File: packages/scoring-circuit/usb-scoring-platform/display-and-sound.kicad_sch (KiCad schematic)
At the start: 14 parts, among them J7 TST-108-02-G-D - HUB75, J8 645004114822 - panel 5V, Q1 BSS138-7-F, Q2 BSS138-7-F, U14 SN74AHCT245PWR, U15 SN74AHCT245PWR

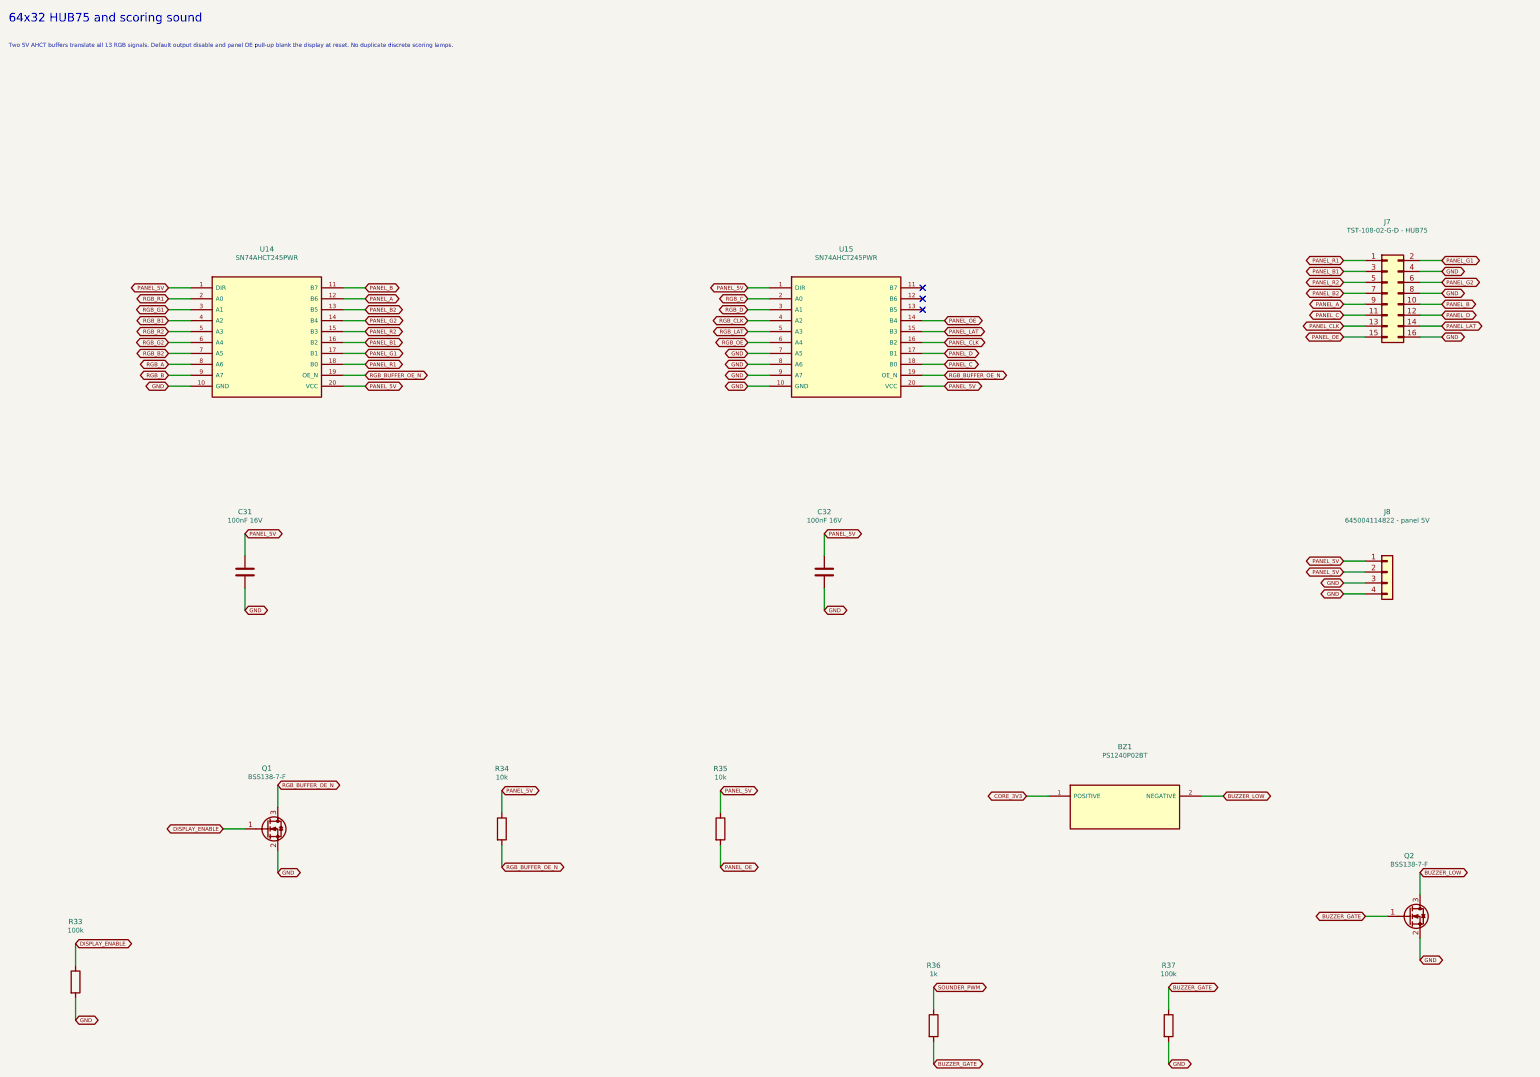
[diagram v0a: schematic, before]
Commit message: fix(scoring-circuit): define HUB75 buffer reset states
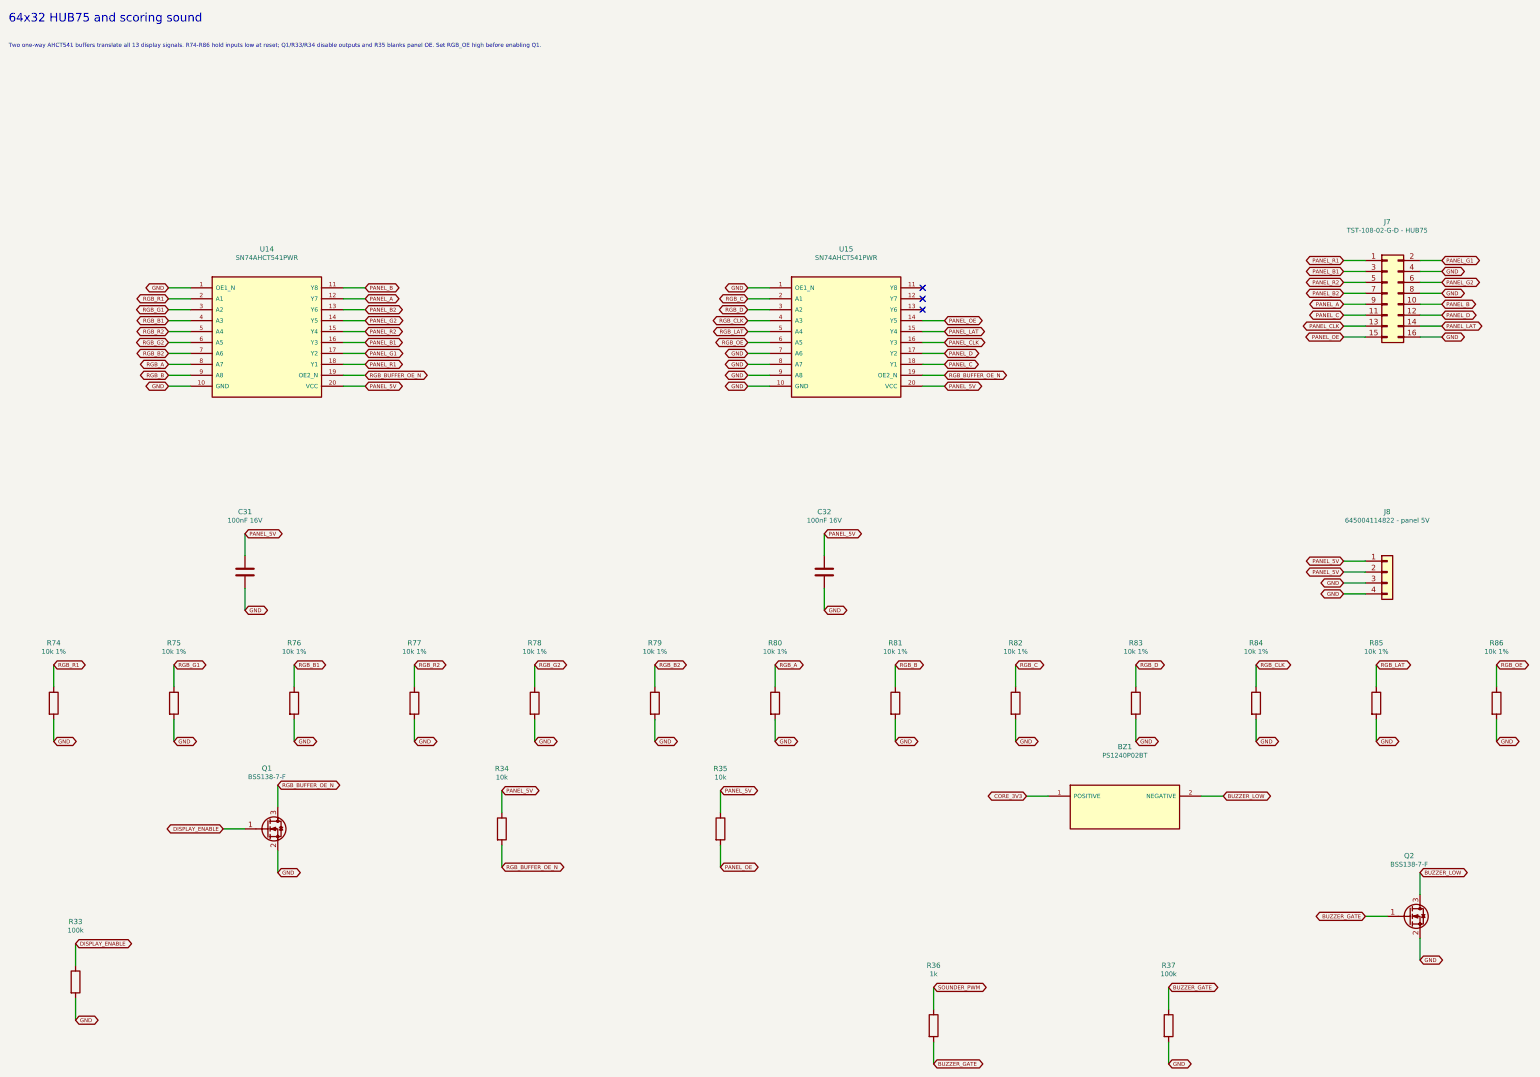
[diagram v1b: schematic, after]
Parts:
- added R74, R75, R76, R77, R78, R79, R80, R81, R82, R83, R84, R85, R86: 10k 1%, Resistor_SMD:R_0603_1608Metric, symbol Device:R
- U14, U15: value SN74AHCT245PWR -> SN74AHCT541PWR; symbol ScoringPlatform:SN74AHCT245PWR -> ScoringPlatform:SN74AHCT541PWR
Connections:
- net GND: now also U14.1 (OE1_N), U15.1 (OE1_N), R74.2, R75.2, R76.2, R77.2, R78.2, R79.2, R80.2, R81.2, R82.2, R83.2, R84.2, R85.2, R86.2
- net PANEL_5V: no longer U14.1 (DIR), U15.1 (DIR)
- net RGB_A: now also R80.1
- net RGB_B: now also R81.1
- net RGB_B1: now also R76.1
- net RGB_B2: now also R79.1
- net RGB_C: now also R82.1
- net RGB_CLK: now also R84.1
- net RGB_D: now also R83.1
- net RGB_G1: now also R75.1
- net RGB_G2: now also R78.1
- net RGB_LAT: now also R85.1
- net RGB_OE: now also R86.1
- net RGB_R1: now also R74.1
- net RGB_R2: now also R77.1
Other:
- note added: "Two one-way AHCT541 buffers translate all 13 display signals. R74-R86 hold inputs low at reset; Q1/R33/R34 disable outputs and R35 blanks panel OE. Set RGB_OE high before enabling Q1."
- note removed: "Two 5V AHCT buffers translate all 13 RGB signals. Default output disable and panel OE pull-up blank the display at reset. No duplicate discrete scoring lamps."

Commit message: fix(scoring-circuit): complete piezo sounder drive and routing
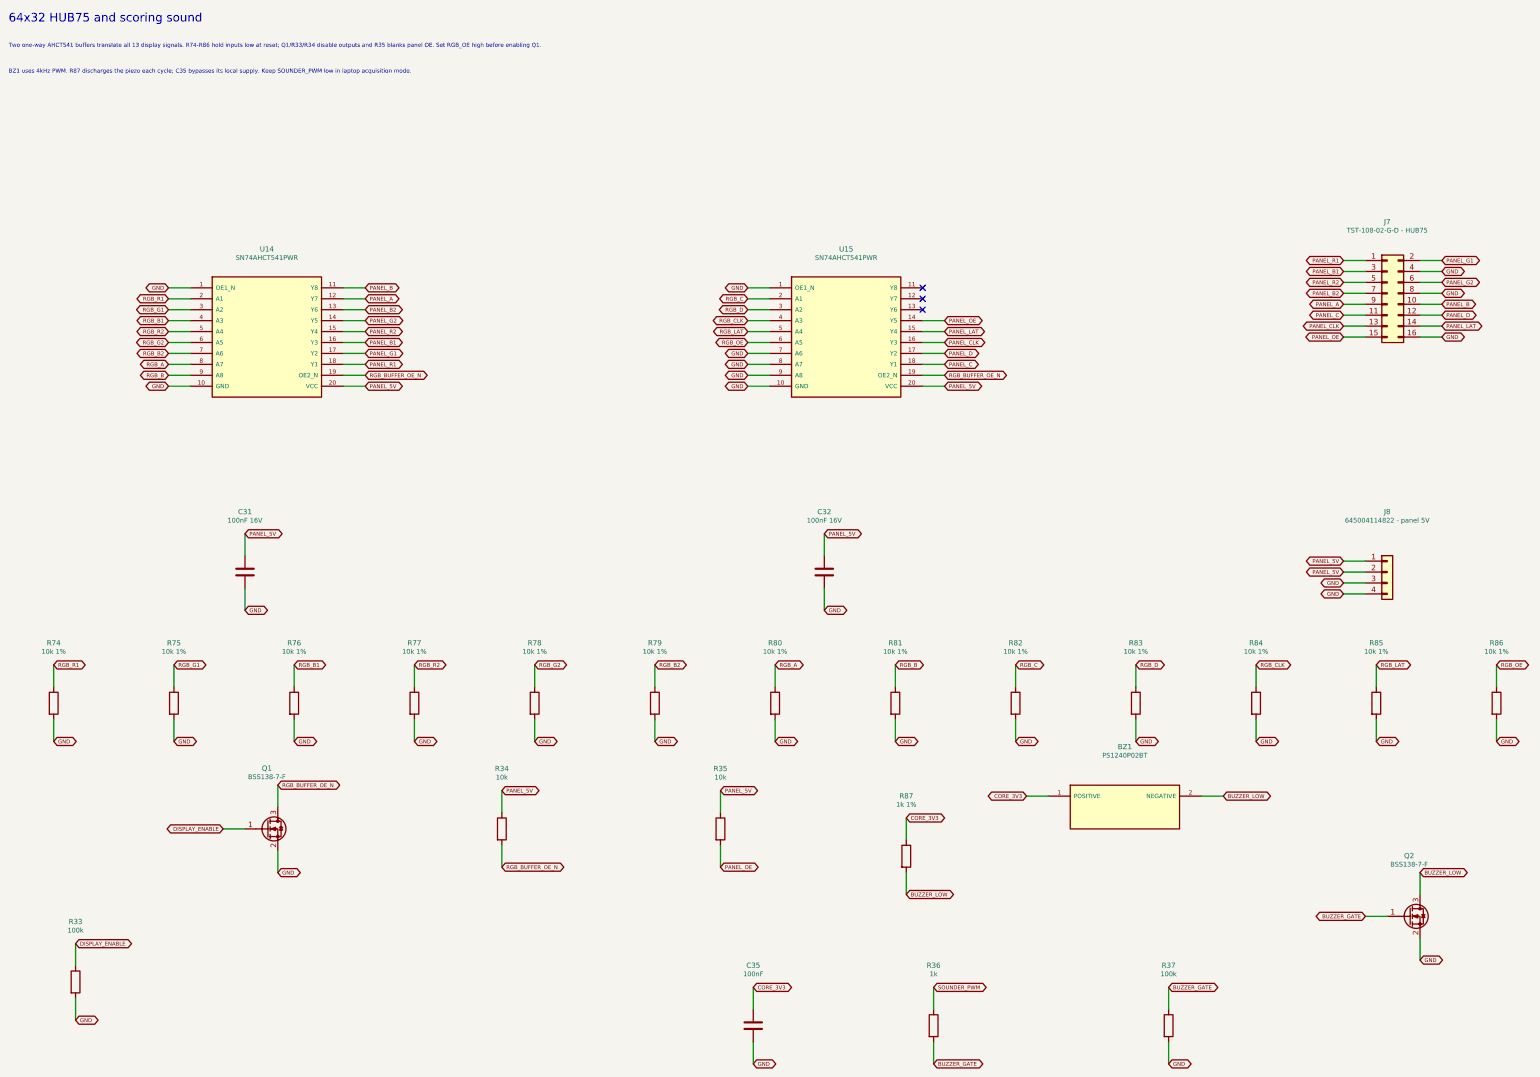
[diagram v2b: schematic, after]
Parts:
- added C35: 100nF, Capacitor_SMD:C_0603_1608Metric, symbol Device:C
- added R87: 1k 1%, Resistor_SMD:R_0603_1608Metric, symbol Device:R
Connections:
- net BUZZER_LOW: now also R87.2
- net CORE_3V3: now also C35.1, R87.1
- net GND: now also C35.2
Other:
- note added: "BZ1 uses 4kHz PWM. R87 discharges the piezo each cycle; C35 bypasses its local supply. Keep SOUNDER_PWM low in laptop acquisition mode."
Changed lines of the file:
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@@
 (global_label "RGB_OE" (shape bidirectional) (at 365.76000000000005 166.37 0) (effects (font (size .9 .9)) (justify left)) (property "Intersheetrefs" "" (at 365.76000000000005 166.37 0) (effects (font (size 1 1)) (hide yes))))
 (wire (pts (xy 365.76000000000005 179.07) (xy 365.76000000000005 184.15)) (stroke (width 0) (type default)))
-(global_label "GND" (shape bidirectional) (at 365.76000000000005 184.15 0) (effects (font (size .9 .9)) (justify left)) (property "Intersheetrefs" "" (at 365.76000000000005 184.15 0) (effects (font (size 1 1)) (hide yes)))))
+(global_label "GND" (shape bidirectional) (at 365.76000000000005 184.15 0) (effects (font (size .9 .9)) (justify left)) (property "Intersheetrefs" "" (at 365.76000000000005 184.15 0) (effects (font (size 1 1)) (hide yes))))
+(symbol (lib_id "Device:R") (at 228.6 210.82 0) (unit 1) (in_bom yes) (on_board yes) (dnp no) (property "Reference" "R87" (at 228.6 196.82 0) (effects (font (size 1.2 1.2)))) (property "Value" "1k 1%" (at 228.6 198.82 0) (effects (font (size 1.1 1.1)))) (property "Footprint" "Resistor_SMD:R_0603_1608Metric" (at 228.6 210.82 0) (effects (font (size 1 1)) (hide yes))) (pin "1") (pin "2") (instances (project "usb-scoring-platform" (path "/20cc8167-128c-446a-a106-f942323e143f/8eb01a97-00e8-4fc9-a0dc-2c04f64b61fc" (reference "R87") (unit 1)))))
+(wire (pts (xy 228.6 207.01) (xy 228.6 201.93)) (stroke (width 0) (type default)))
+(global_label "CORE_3V3" (shape bidirectional) (at 228.6 201.93 0) (effects (font (size .9 .9)) (justify left)) (property "Intersheetrefs" "" (at 228.6 201.93 0) (effects (font (size 1 1)) (hide yes))))
+(wire (pts (xy 228.6 214.63) (xy 228.6 219.71)) (stroke (width 0) (type default)))
+(global_label "BUZZER_LOW" (shape bidirectional) (at 228.6 219.71 0) (effects (font (size .9 .9)) (justify left)) (property "Intersheetrefs" "" (at 228.6 219.71 0) (effects (font (size 1 1)) (hide yes))))
+(symbol (lib_id "Device:C") (at 193.04 250.19 0) (unit 1) (in_bom yes) (on_board yes) (dnp no) (property "Reference" "C35" (at 193.04 236.19 0) (effects (font (size 1.2 1.2)))) (property "Value" "100nF" (at 193.04 238.19 0) (effects (font (size 1.1 1.1)))) (property "Footprint" "Capacitor_SMD:C_0603_1608Metric" (at 193.04 250.19 0) (effects (font (size 1 1)) (hide yes))) (pin "1") (pin "2") (instances (project "usb-scoring-platform" (path "/20cc8167-128c-446a-a106-f942323e143f/8eb01a97-00e8-4fc9-a0dc-2c04f64b61fc" (reference "C35") (unit 1)))))
+(wire (pts (xy 193.04 246.38) (xy 193.04 241.3)) (stroke (width 0) (type default)))
+(global_label "CORE_3V3" (shape bidirectional) (at 193.04 241.3 0) (effects (font (size .9 .9)) (justify left)) (property "Intersheetrefs" "" (at 193.04 241.3 0) (effects (font (size 1 1)) (hide yes))))
+(wire (pts (xy 193.04 254) (xy 193.04 259.08)) (stroke (width 0) (type default)))
+(global_label "GND" (shape bidirectional) (at 193.04 259.08 0) (effects (font (size .9 .9)) (justify left)) (property "Intersheetrefs" "" (at 193.04 259.08 0) (effects (font (size 1 1)) (hide yes))))
+(text "BZ1 uses 4kHz PWM. R87 discharges the piezo each cycle; C35 bypasses its local supply. Keep SOUNDER_PWM low in laptop acquisition mode." (at 20 28 0) (effects (font (size .95 .95)) (justify left top))))

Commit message: feat(scoring-circuit): select exact prototype resistor parts
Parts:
- R33, R37: MPN (none) -> RC0603FR-07100KL; Manufacturer (none) -> YAGEO
- R34, R35, R74, R75, R76, R77, R78, R79, R80, R81, R82, R83, R84, R85, R86: MPN (none) -> RC0603FR-0710KL; Manufacturer (none) -> YAGEO
- R36, R87: MPN (none) -> RC0603FR-071KL; Manufacturer (none) -> YAGEO

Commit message: feat(scoring-circuit): select bypass and timing capacitors
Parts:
- C31, C32, C35: MPN (none) -> C1608X7R1H104K080AA; Manufacturer (none) -> TDK
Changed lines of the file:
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@@
 (wire (pts (xy 97.79 101.6) (xy 102.87 101.6)) (stroke (width 0) (type default)))
 (global_label "PANEL_5V" (shape bidirectional) (at 102.87 101.6 0) (effects (font (size 0.9 0.9)) (justify left)) (property "Intersheetrefs" "" (at 102.87 101.6 0) (effects (font (size 1 1)) (hide yes))))
-(symbol (lib_id "Device:C") (at 74.93 144.78 0) (unit 1) (in_bom yes) (on_board yes) (dnp no) (property "Reference" "C31" (at 74.93 130.78 0) (effects (font (size 1.2 1.2)))) (property "Value" "100nF 16V" (at 74.93 132.78 0) (effects (font (size 1.1 1.1)))) (property "Footprint" "Capacitor_SMD:C_0603_1608Metric" (at 74.93 144.78 0) (effects (font (size 1 1)) (hide yes))) (pin "1") (pin "2") (instances (project "usb-scoring-platform" (path "/20cc8167-128c-446a-a106-f942323e143f/8eb01a97-00e8-4fc9-a0dc-2c04f64b61fc" (reference "C31") (unit 1)))))
+(symbol (lib_id "Device:C") (at 74.93 144.78 0) (unit 1) (in_bom yes) (on_board yes) (dnp no) (property "Reference" "C31" (at 74.93 130.78 0) (effects (font (size 1.2 1.2)))) (property "Value" "100nF 16V" (at 74.93 132.78 0) (effects (font (size 1.1 1.1)))) (property "Footprint" "Capacitor_SMD:C_0603_1608Metric" (at 74.93 144.78 0) (effects (font (size 1 1)) (hide yes))) (pin "1") (pin "2") (property "Manufacturer" "TDK" (at 74.93 144.78 0) (effects (font (size 1 1)) (hide yes))) (property "MPN" "C1608X7R1H104K080AA" (at 74.93 144.78 0) (effects (font (size 1 1)) (hide yes))) (property "Datasheet" "https://product.tdk.com/en/search/capacitor/ceramic/mlcc/info?part_no=C1608X7R1H104K080AA" (at 74.93 144.78 0) (effects (font (size 1 1)) (hide yes))) (instances (project "usb-scoring-platform" (path "/20cc8167-128c-446a-a106-f942323e143f/8eb01a97-00e8-4fc9-a0dc-2c04f64b61fc" (reference "C31") (unit 1)))))
 (wire (pts (xy 74.93 140.97) (xy 74.93 135.89)) (stroke (width 0) (type default)))
 (global_label "PANEL_5V" (shape bidirectional) (at 74.93 135.89 0) (effects (font (size 0.9 0.9)) (justify left)) (property "Intersheetrefs" "" (at 74.93 135.89 0) (effects (font (size 1 1)) (hide yes))))
@@
 (wire (pts (xy 232.41 101.6) (xy 237.49 101.6)) (stroke (width 0) (type default)))
 (global_label "PANEL_5V" (shape bidirectional) (at 237.49 101.6 0) (effects (font (size 0.9 0.9)) (justify left)) (property "Intersheetrefs" "" (at 237.49 101.6 0) (effects (font (size 1 1)) (hide yes))))
-(symbol (lib_id "Device:C") (at 209.55 144.78 0) (unit 1) (in_bom yes) (on_board yes) (dnp no) (property "Reference" "C32" (at 209.55 130.78 0) (effects (font (size 1.2 1.2)))) (property "Value" "100nF 16V" (at 209.55 132.78 0) (effects (font (size 1.1 1.1)))) (property "Footprint" "Capacitor_SMD:C_0603_1608Metric" (at 209.55 144.78 0) (effects (font (size 1 1)) (hide yes))) (pin "1") (pin "2") (instances (project "usb-scoring-platform" (path "/20cc8167-128c-446a-a106-f942323e143f/8eb01a97-00e8-4fc9-a0dc-2c04f64b61fc" (reference "C32") (unit 1)))))
+(symbol (lib_id "Device:C") (at 209.55 144.78 0) (unit 1) (in_bom yes) (on_board yes) (dnp no) (property "Reference" "C32" (at 209.55 130.78 0) (effects (font (size 1.2 1.2)))) (property "Value" "100nF 16V" (at 209.55 132.78 0) (effects (font (size 1.1 1.1)))) (property "Footprint" "Capacitor_SMD:C_0603_1608Metric" (at 209.55 144.78 0) (effects (font (size 1 1)) (hide yes))) (pin "1") (pin "2") (property "Manufacturer" "TDK" (at 209.55 144.78 0) (effects (font (size 1 1)) (hide yes))) (property "MPN" "C1608X7R1H104K080AA" (at 209.55 144.78 0) (effects (font (size 1 1)) (hide yes))) (property "Datasheet" "https://product.tdk.com/en/search/capacitor/ceramic/mlcc/info?part_no=C1608X7R1H104K080AA" (at 209.55 144.78 0) (effects (font (size 1 1)) (hide yes))) (instances (project "usb-scoring-platform" (path "/20cc8167-128c-446a-a106-f942323e143f/8eb01a97-00e8-4fc9-a0dc-2c04f64b61fc" (reference "C32") (unit 1)))))
 (wire (pts (xy 209.55 140.97) (xy 209.55 135.89)) (stroke (width 0) (type default)))
 (global_label "PANEL_5V" (shape bidirectional) (at 209.55 135.89 0) (effects (font (size 0.9 0.9)) (justify left)) (property "Intersheetrefs" "" (at 209.55 135.89 0) (effects (font (size 1 1)) (hide yes))))
@@
 (wire (pts (xy 228.6 214.63) (xy 228.6 219.71)) (stroke (width 0) (type default)))
 (global_label "BUZZER_LOW" (shape bidirectional) (at 228.6 219.71 0) (effects (font (size .9 .9)) (justify left)) (property "Intersheetrefs" "" (at 228.6 219.71 0) (effects (font (size 1 1)) (hide yes))))
-(symbol (lib_id "Device:C") (at 193.04 250.19 0) (unit 1) (in_bom yes) (on_board yes) (dnp no) (property "Reference" "C35" (at 193.04 236.19 0) (effects (font (size 1.2 1.2)))) (property "Value" "100nF" (at 193.04 238.19 0) (effects (font (size 1.1 1.1)))) (property "Footprint" "Capacitor_SMD:C_0603_1608Metric" (at 193.04 250.19 0) (effects (font (size 1 1)) (hide yes))) (pin "1") (pin "2") (instances (project "usb-scoring-platform" (path "/20cc8167-128c-446a-a106-f942323e143f/8eb01a97-00e8-4fc9-a0dc-2c04f64b61fc" (reference "C35") (unit 1)))))
+(symbol (lib_id "Device:C") (at 193.04 250.19 0) (unit 1) (in_bom yes) (on_board yes) (dnp no) (property "Reference" "C35" (at 193.04 236.19 0) (effects (font (size 1.2 1.2)))) (property "Value" "100nF" (at 193.04 238.19 0) (effects (font (size 1.1 1.1)))) (property "Footprint" "Capacitor_SMD:C_0603_1608Metric" (at 193.04 250.19 0) (effects (font (size 1 1)) (hide yes))) (pin "1") (pin "2") (property "Manufacturer" "TDK" (at 193.04 250.19 0) (effects (font (size 1 1)) (hide yes))) (property "MPN" "C1608X7R1H104K080AA" (at 193.04 250.19 0) (effects (font (size 1 1)) (hide yes))) (property "Datasheet" "https://product.tdk.com/en/search/capacitor/ceramic/mlcc/info?part_no=C1608X7R1H104K080AA" (at 193.04 250.19 0) (effects (font (size 1 1)) (hide yes))) (instances (project "usb-scoring-platform" (path "/20cc8167-128c-446a-a106-f942323e143f/8eb01a97-00e8-4fc9-a0dc-2c04f64b61fc" (reference "C35") (unit 1)))))
 (wire (pts (xy 193.04 246.38) (xy 193.04 241.3)) (stroke (width 0) (type default)))
 (global_label "CORE_3V3" (shape bidirectional) (at 193.04 241.3 0) (effects (font (size .9 .9)) (justify left)) (property "Intersheetrefs" "" (at 193.04 241.3 0) (effects (font (size 1 1)) (hide yes))))
